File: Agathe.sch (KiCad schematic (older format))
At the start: 177 parts, among them J1 Conn_01x04_Female, J3 AVR-ISP-6, SW1 SW_Push, U1 ATmega32U4-AU, U2 PRTR5V0U2X, Y1 16MHz

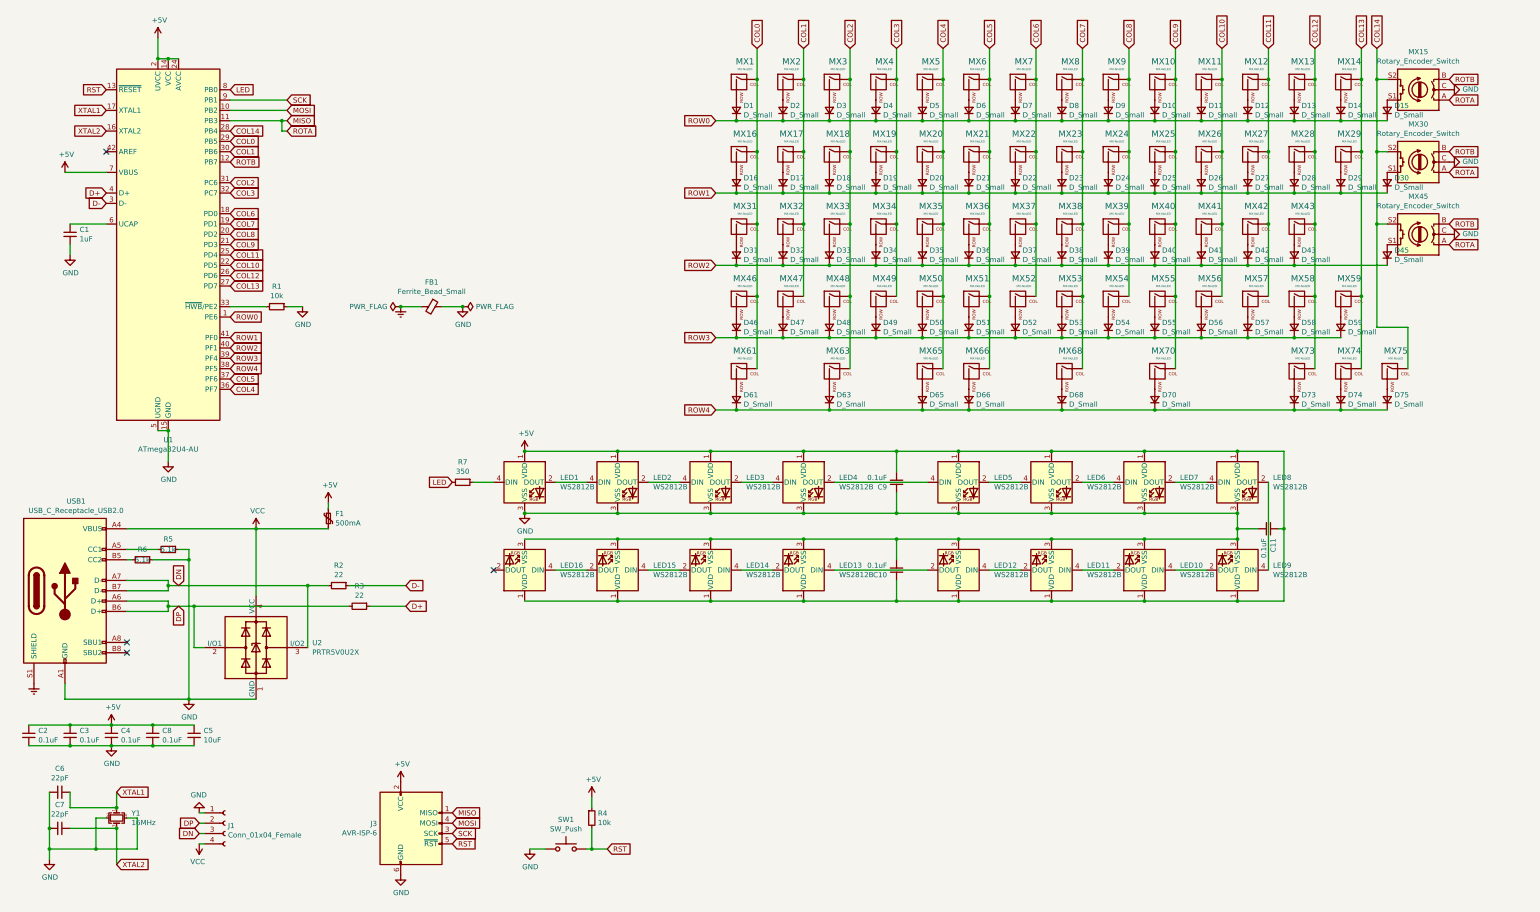
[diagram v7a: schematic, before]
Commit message: add a breakable usb port and matrix encoder
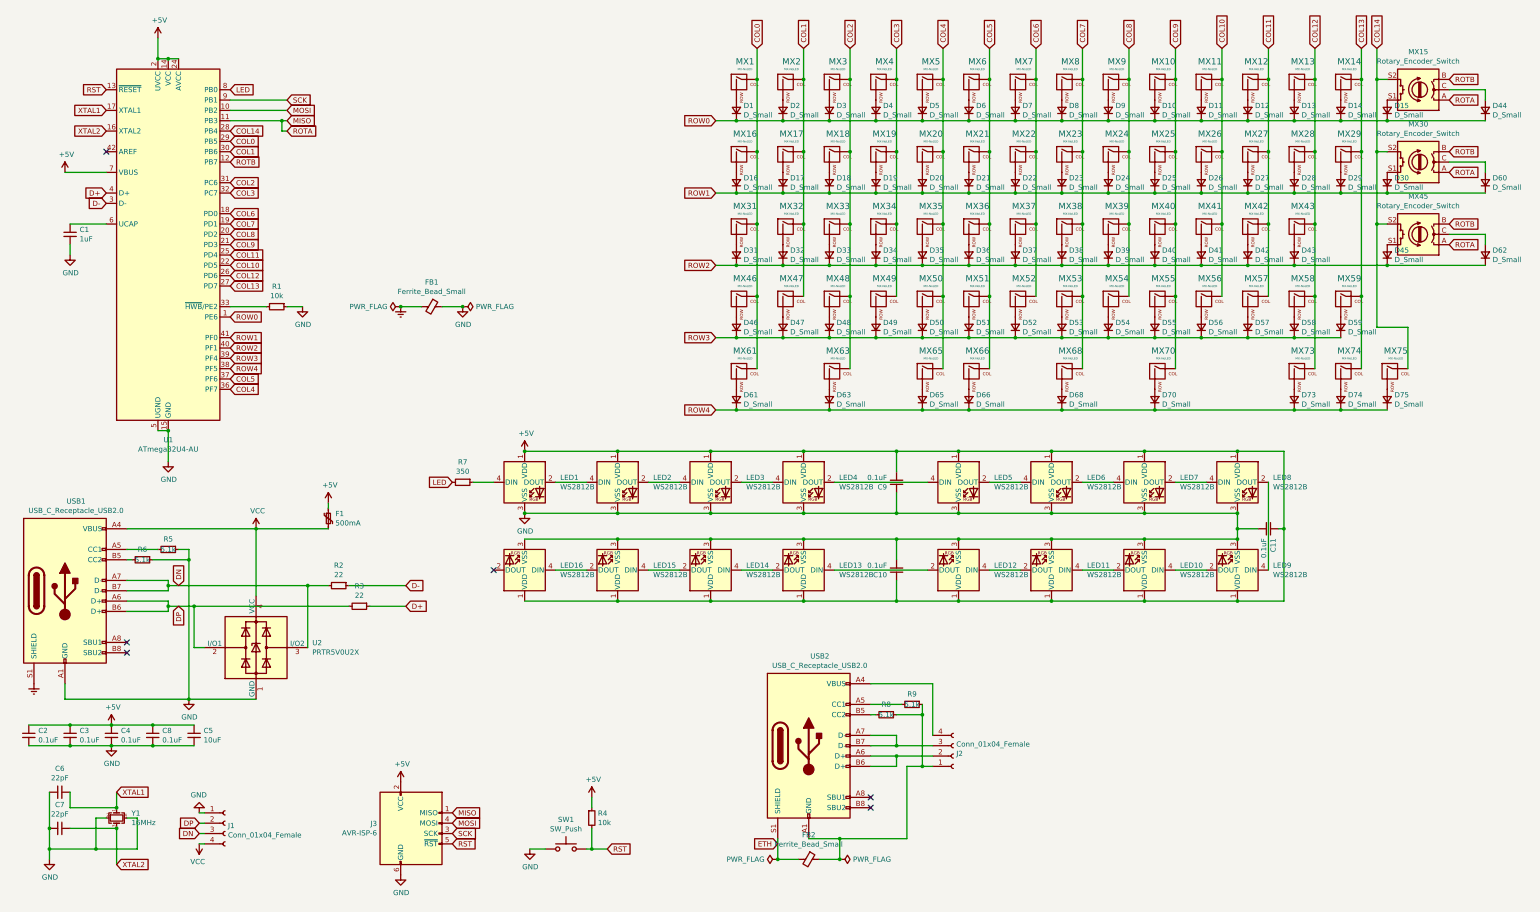
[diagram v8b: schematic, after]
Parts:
- added D44, D60, D62: D_Small, Diode_SMD:D_SOD-123, symbol Device:D_Small
- added FB2: Ferrite_Bead_Small, Inductor_SMD:L_0805_2012Metric_Pad1.15x1.40mm_HandSolder, symbol Device:Ferrite_Bead_Small
- added J2: Conn_01x04_Female, Connector_PinHeader_2.54mm:PinHeader_1x04_P2.54mm_Vertical, symbol Connector:Conn_01x04_Female
- added R8, R9: 5.1k, Resistor_SMD:R_0805_2012Metric, symbol Device:R_Small
- added USB2: USB_C_Receptacle_USB2.0, Connector_USB:USB_C_Receptacle_HRO_TYPE-C-31-M-12, symbol Connector:USB_C_Receptacle_USB2.0
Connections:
- net GND: no longer MX15.C, MX30.C, MX45.C
- net ROW0: now also D44.1 (K)
- net ROW1: now also D60.1 (K)
- net ROW2: now also D62.1 (K)
- new net: D44.2 (A), MX15.C
- new net: D60.2 (A), MX30.C
- new net: D62.2 (A), MX45.C
- new net: FB2.1, J2.1 (Pin_1), R8.1, R9.1, USB2.A1 (GND), USB2.A12 (GND), USB2.B1 (GND), USB2.B12 (GND)
- new net: J2.4 (Pin_4), USB2.A4 (VBUS), USB2.A9 (VBUS), USB2.B4 (VBUS), USB2.B9 (VBUS)
- new net: R9.2, USB2.A5 (CC1)
- new net: J2.2 (Pin_2), USB2.A6 (D+), USB2.B6 (D+)
- new net: J2.3 (Pin_3), USB2.A7 (D-), USB2.B7 (D-)
- new net: R8.2, USB2.B5 (CC2)
- new net ETH: FB2.2, USB2.S1 (SHIELD)
- no-connect marks 4 -> 6
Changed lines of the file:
@@
 	13950 3500 13950 3900
 Connection ~ 13650 2500
-$Comp
-L power:GND #PWR0113
-U 1 1 5EBCE257
-P 14350 1200
-F 0 "#PWR0113" H 14350 950 50  0001 C CNN
-F 1 "GND" V 14355 1072 50  0000 R CNN
-F 2 "" H 14350 1200 50  0001 C CNN
-F 3 "" H 14350 1200 50  0001 C CNN
-	1    14350 1200
-	0    -1   -1   0
-$EndComp
-$Comp
-L power:GND #PWR0115
-U 1 1 5EBCE8DB
-P 14350 1900
-F 0 "#PWR0115" H 14350 1650 50  0001 C CNN
-F 1 "GND" V 14355 1772 50  0000 R CNN
-F 2 "" H 14350 1900 50  0001 C CNN
-F 3 "" H 14350 1900 50  0001 C CNN
-	1    14350 1900
-	0    -1   -1   0
-$EndComp
-$Comp
-L power:GND #PWR0116
-U 1 1 5EBCEE25
-P 14350 2600
-F 0 "#PWR0116" H 14350 2350 50  0001 C CNN
-F 1 "GND" V 14355 2472 50  0000 R CNN
-F 2 "" H 14350 2600 50  0001 C CNN
-F 3 "" H 14350 2600 50  0001 C CNN
-	1    14350 2600
-	0    -1   -1   0
-$EndComp
 Text GLabel 14350 1300 2    50   Input ~ 0
 ROTA
@@
 Text GLabel 2550 2400 2    50   Input ~ 0
 COL6
-$Comp
-L Connector:Conn_01x04_Female J1
-U 1 1 5F7DB4E9
-P 2500 8300
-F 0 "J1" H 2528 8276 50  0000 L CNN
-F 1 "Conn_01x04_Female" H 2528 8185 50  0000 L CNN
-F 2 "Connector_PinHeader_2.54mm:PinHeader_1x04_P2.54mm_Vertical" H 2500 8300 50  0001 C CNN
-F 3 "~" H 2500 8300 50  0001 C CNN
-	1    2500 8300
-	1    0    0    -1
-$EndComp
-Text GLabel 2250 8400 0    50   Input ~ 0
-DN
-Text GLabel 2250 8300 0    50   Input ~ 0
-DP
-Wire Wire Line
-	2300 8200 2250 8200
-Wire Wire Line
-	2300 8300 2250 8300
-Wire Wire Line
-	2300 8400 2250 8400
-Wire Wire Line
-	2250 8500 2300 8500
-$Comp
-L power:GND #PWR02
-U 1 1 5F8431E2
-P 2250 8200
-F 0 "#PWR02" H 2250 7950 50  0001 C CNN
-F 1 "GND" H 2255 8027 50  0000 C CNN
-F 2 "" H 2250 8200 50  0001 C CNN
-F 3 "" H 2250 8200 50  0001 C CNN
-	1    2250 8200
-	-1   0    0    1
-$EndComp
-$Comp
-L power:VCC #PWR01
-U 1 1 5F84490E
-P 2250 8500
-F 0 "#PWR01" H 2250 8350 50  0001 C CNN
-F 1 "VCC" H 2265 8673 50  0000 C CNN
-F 2 "" H 2250 8500 50  0001 C CNN
-F 3 "" H 2250 8500 50  0001 C CNN
-	1    2250 8500
-	-1   0    0    1
-$EndComp
 Connection ~ 1950 900
 Connection ~ 1850 900
@@
 Connection ~ 9000 6150
 Connection ~ 9600 6150
+$Comp
+L power:VCC #PWR01
+U 1 1 5F84490E
+P 2250 8500
+F 0 "#PWR01" H 2250 8350 50  0001 C CNN
+F 1 "VCC" H 2265 8673 50  0000 C CNN
+F 2 "" H 2250 8500 50  0001 C CNN
+F 3 "" H 2250 8500 50  0001 C CNN
+	1    2250 8500
+	-1   0    0    1
+$EndComp
+$Comp
+L power:GND #PWR02
+U 1 1 5F8431E2
+P 2250 8200
+F 0 "#PWR02" H 2250 7950 50  0001 C CNN
+F 1 "GND" H 2255 8027 50  0000 C CNN
+F 2 "" H 2250 8200 50  0001 C CNN
+F 3 "" H 2250 8200 50  0001 C CNN
+	1    2250 8200
+	-1   0    0    1
+$EndComp
+Wire Wire Line
+	2250 8500 2300 8500
+Wire Wire Line
+	2300 8400 2250 8400
+Wire Wire Line
+	2300 8300 2250 8300
+Wire Wire Line
+	2300 8200 2250 8200
+Text GLabel 2250 8300 0    50   Input ~ 0
+DP
+Text GLabel 2250 8400 0    50   Input ~ 0
+DN
+$Comp
+L Connector:Conn_01x04_Female J1
+U 1 1 5F7DB4E9
+P 2500 8300
+F 0 "J1" H 2528 8276 50  0000 L CNN
+F 1 "Conn_01x04_Female" H 2528 8185 50  0000 L CNN
+F 2 "Connector_PinHeader_2.54mm:PinHeader_1x04_P2.54mm_Vertical" H 2500 8300 50  0001 C CNN
+F 3 "~" H 2500 8300 50  0001 C CNN
+	1    2500 8300
+	1    0    0    -1
+$EndComp
+Wire Wire Line
+	8750 7650 9000 7650
+Wire Wire Line
+	9000 7650 9000 7750
+Wire Wire Line
+	9000 7750 8750 7750
+Connection ~ 9000 7650
+Wire Wire Line
+	8750 7550 9000 7550
+Wire Wire Line
+	8750 7450 9000 7450
+Wire Wire Line
+	9000 7450 9000 7550
+Connection ~ 9000 7550
+Wire Wire Line
+	8150 8450 8450 8450
+Wire Wire Line
+	9100 8450 9100 7750
+NoConn ~ 8750 8050
+NoConn ~ 8750 8150
+$Comp
+L Device:R_Small R9
+U 1 1 601A8B7C
+P 9150 7150
+F 0 "R9" V 9050 7150 50  0000 C CNN
+F 1 "5.1k" V 9150 7150 50  0000 C CNN
+F 2 "Resistor_SMD:R_0805_2012Metric" H 9150 7150 50  0001 C CNN
+F 3 "~" H 9150 7150 50  0001 C CNN
+	1    9150 7150
+	0    1    1    0
+$EndComp
+Wire Wire Line
+	9050 7150 8750 7150
+Wire Wire Line
+	8800 7250 8750 7250
+$Comp
+L Device:R_Small R8
+U 1 1 601A8B85
+P 8900 7250
+F 0 "R8" V 8800 7250 50  0000 C CNN
+F 1 "5.1k" V 8900 7250 50  0000 C CNN
+F 2 "Resistor_SMD:R_0805_2012Metric" H 8900 7250 50  0001 C CNN
+F 3 "~" H 8900 7250 50  0001 C CNN
+	1    8900 7250
+	0    1    1    0
+$EndComp
+Wire Wire Line
+	9250 7250 9250 7150
+Wire Wire Line
+	9000 7250 9250 7250
+Wire Wire Line
+	9000 7550 9350 7550
+Wire Wire Line
+	9000 7650 9350 7650
+Wire Wire Line
+	9100 7750 9250 7750
+$Comp
+L Connector:Conn_01x04_Female J2
+U 1 1 600557B3
+P 9550 7650
+F 0 "J2" H 9578 7626 50  0000 L CNN
+F 1 "Conn_01x04_Female" H 9578 7535 50  0000 L CNN
+F 2 "Connector_PinHeader_2.54mm:PinHeader_1x04_P2.54mm_Vertical" H 9550 7650 50  0001 C CNN
+F 3 "~" H 9550 7650 50  0001 C CNN
+	1    9550 7650
+	1    0    0    1
+$EndComp
+Wire Wire Line
+	9250 7250 9250 7750
+Connection ~ 9250 7250
+Connection ~ 9250 7750
+Wire Wire Line
+	9250 7750 9350 7750
+Wire Wire Line
+	9350 6950 9350 7450
+Wire Wire Line
+	8750 6950 9350 6950
+$Comp
+L Device:Ferrite_Bead_Small FB2
+U 1 1 602B3308
+P 8150 8650
+F 0 "FB2" V 7913 8650 50  0000 C CNN
+F 1 "Ferrite_Bead_Small" V 8004 8650 50  0000 C CNN
+F 2 "Inductor_SMD:L_0805_2012Metric_Pad1.15x1.40mm_HandSolder" V 8080 8650 50  0001 C CNN
+F 3 "~" H 8150 8650 50  0001 C CNN
+	1    8150 8650
+	0    1    1    0
+$EndComp
+Wire Wire Line
+	8250 8650 8450 8650
+Wire Wire Line
+	8050 8650 7850 8650
+$Comp
+L power:PWR_FLAG #FLG0103
+U 1 1 602B3316
+P 8450 8650
+F 0 "#FLG0103" H 8450 8725 50  0001 C CNN
+F 1 "PWR_FLAG" V 8450 8778 50  0000 L CNN
+F 2 "" H 8450 8650 50  0001 C CNN
+F 3 "~" H 8450 8650 50  0001 C CNN
+	1    8450 8650
+	0    1    1    0
+$EndComp
+$Comp
+L power:PWR_FLAG #FLG0104
+U 1 1 602B331D
+P 7850 8650
+F 0 "#FLG0104" H 7850 8725 50  0001 C CNN
+F 1 "PWR_FLAG" V 7850 8777 50  0000 L CNN
+F 2 "" H 7850 8650 50  0001 C CNN
+F 3 "~" H 7850 8650 50  0001 C CNN
+	1    7850 8650
+	0    -1   -1   0
+$EndComp
+$Comp
+L Connector:USB_C_Receptacle_USB2.0 USB2
+U 1 1 5FD41509
+P 8150 7550
+F 0 "USB2" H 8257 8417 50  0000 C CNN
+F 1 "USB_C_Receptacle_USB2.0" H 8257 8326 50  0000 C CNN
+F 2 "Connector_USB:USB_C_Receptacle_HRO_TYPE-C-31-M-12" H 8300 7550 50  0001 C CNN
+F 3 "https://www.usb.org/sites/default/files/documents/usb_type-c.zip" H 8300 7550 50  0001 C CNN
+	1    8150 7550
+	1    0    0    -1
+$EndComp
+Wire Wire Line
+	7850 8450 7850 8650
+Connection ~ 7850 8650
+Wire Wire Line
+	8450 8650 8450 8450
+Connection ~ 8450 8650
+Connection ~ 8450 8450
+Wire Wire Line
+	8450 8450 9100 8450
+Text GLabel 7850 8500 0    50   Input ~ 0
+ETH
+$Comp
+L Device:D_Small D62
+U 1 1 603BD856
+P 14700 2800
+F 0 "D62" V 14746 2730 50  0000 R CNN
+F 1 "D_Small" V 14655 2730 50  0000 R CNN
+F 2 "Diode_SMD:D_SOD-123" V 14700 2800 50  0001 C CNN
+F 3 "~" V 14700 2800 50  0001 C CNN
+	1    14700 2800
+	0    -1   -1   0
+$EndComp
+Wire Wire Line
+	14350 2600 14700 2600
+Wire Wire Line
+	14700 2600 14700 2700
+Wire Wire Line
+	14700 2900 13750 2900
+Connection ~ 13750 2900
+$Comp
+L Device:D_Small D60
+U 1 1 603F9CA7
+P 14700 2100
+F 0 "D60" V 14746 2030 50  0000 R CNN
+F 1 "D_Small" V 14655 2030 50  0000 R CNN
+F 2 "Diode_SMD:D_SOD-123" V 14700 2100 50  0001 C CNN
+F 3 "~" V 14700 2100 50  0001 C CNN
+	1    14700 2100
+	0    -1   -1   0
+$EndComp
+$Comp
+L Device:D_Small D44
+U 1 1 603FA36B
+P 14700 1400
+F 0 "D44" V 14746 1330 50  0000 R CNN
+F 1 "D_Small" V 14655 1330 50  0000 R CNN
+F 2 "Diode_SMD:D_SOD-123" V 14700 1400 50  0001 C CNN
+F 3 "~" V 14700 1400 50  0001 C CNN
+	1    14700 1400
+	0    -1   -1   0
+$EndComp
+Wire Wire Line
+	13750 2200 14700 2200
+Connection ~ 13750 2200
+Wire Wire Line
+	14700 2000 14700 1900
+Wire Wire Line
+	14700 1900 14350 1900
+Wire Wire Line
+	14350 1200 14700 1200
+Wire Wire Line
+	14700 1200 14700 1300
+Wire Wire Line
+	14700 1500 13750 1500
+Connection ~ 13750 1500
 $EndSCHEMATC
